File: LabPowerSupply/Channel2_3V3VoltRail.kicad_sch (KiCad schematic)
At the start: 8 parts

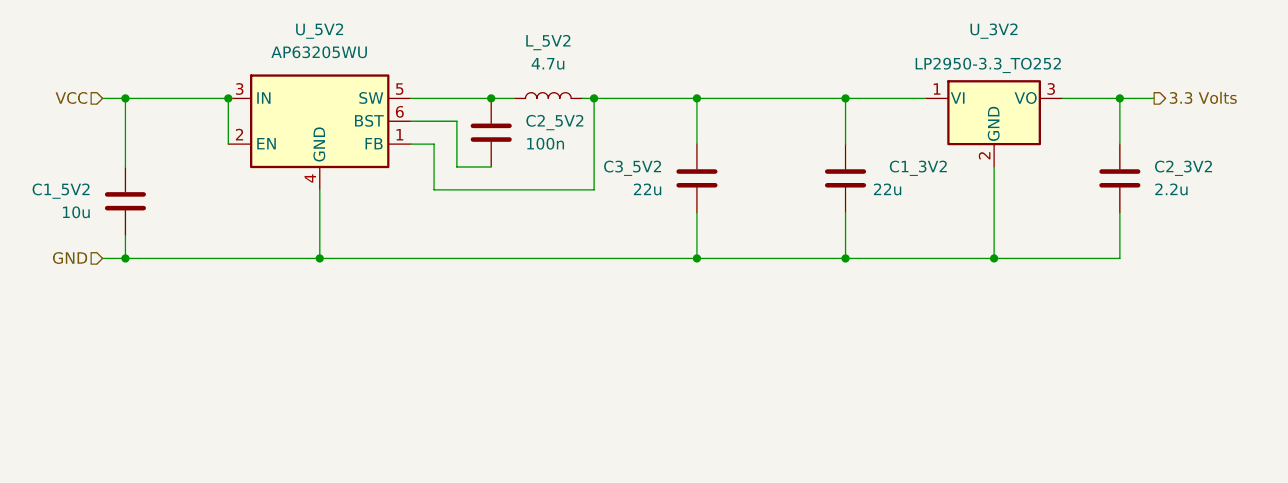
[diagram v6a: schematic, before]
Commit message: Updated Part List
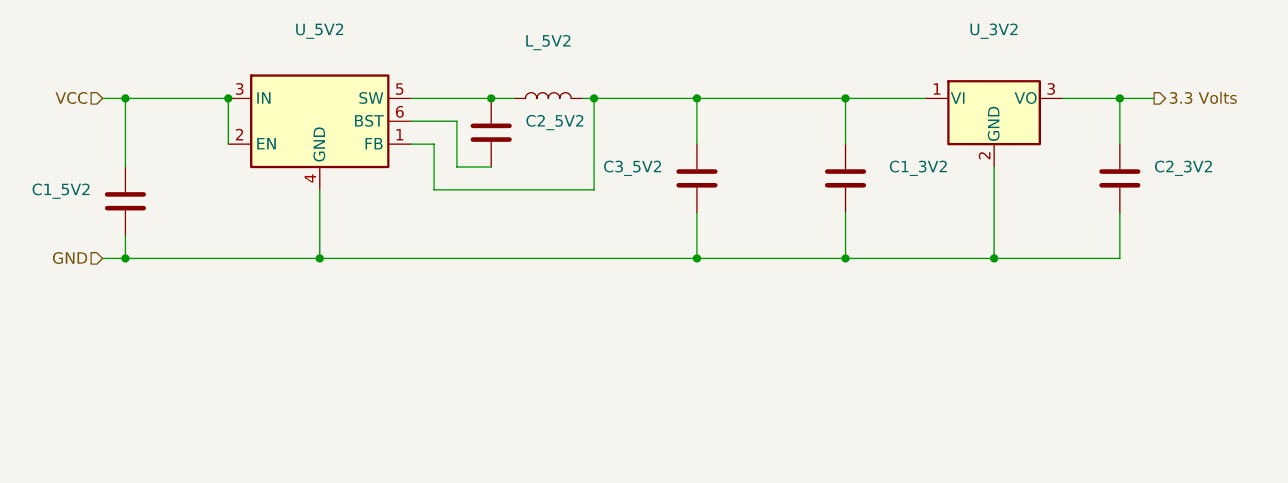
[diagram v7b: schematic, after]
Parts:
- C1_3V2, C3_5V2: value 22u -> (none); footprint Capacitor_SMD:C_1210_3225Metric -> (none)
- C1_5V2: value 10u -> (none); footprint Capacitor_SMD:C_1206_3216Metric -> (none)
- C2_3V2: value 2.2u -> (none); footprint Capacitor_SMD:C_0805_2012Metric -> (none)
- C2_5V2: value 100n -> (none); footprint Capacitor_SMD:C_0603_1608Metric -> (none)
- L_5V2: value 4.7u -> (none); footprint Inductor_SMD:L_Sumida_CDMC6D28_7.25x6.5mm -> (none)
- U_3V2: value LP2950-3.3_TO252 -> (none); footprint Package_TO_SOT_SMD:TO-252-2 -> (none)
- U_5V2: value AP63205WU -> (none); footprint Package_TO_SOT_SMD:TSOT-23-6 -> (none)
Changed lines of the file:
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@@
       (effects (font (size 1.27 1.27)) (justify left))
     )
-    (property "Value" "100n" (id 1) (at 160.02 74.9299 0)
+    (property "Value" "" (id 1) (at 160.02 74.9299 0)
       (effects (font (size 1.27 1.27)) (justify left))
     )
-    (property "Footprint" "Capacitor_SMD:C_0603_1608Metric" (id 2) (at 157.1752 77.47 0)
+    (property "Footprint" "" (id 2) (at 157.1752 77.47 0)
       (effects (font (size 1.27 1.27)) hide)
     )
@@
     (in_bom yes) (on_board yes) (fields_autoplaced)
     (property "Reference" "U_5V2" (id 0) (at 137.16 62.23 0))
-    (property "Value" "AP63205WU" (id 1) (at 137.16 64.77 0))
-    (property "Footprint" "Package_TO_SOT_SMD:TSOT-23-6" (id 2) (at 137.16 95.25 0)
+    (property "Value" "" (id 1) (at 137.16 64.77 0))
+    (property "Footprint" "" (id 2) (at 137.16 95.25 0)
       (effects (font (size 1.27 1.27)) hide)
     )
@@
       (effects (font (size 1.27 1.27)) (justify right))
     )
-    (property "Value" "22u" (id 1) (at 201.93 80.01 0)
+    (property "Value" "" (id 1) (at 201.93 80.01 0)
       (effects (font (size 1.27 1.27)) (justify right))
     )
-    (property "Footprint" "Capacitor_SMD:C_1210_3225Metric" (id 2) (at 196.5452 74.93 0)
+    (property "Footprint" "" (id 2) (at 196.5452 74.93 0)
       (effects (font (size 1.27 1.27)) hide)
     )
@@
     (in_bom yes) (on_board yes)
     (property "Reference" "U_3V2" (id 0) (at 212.09 62.23 0))
-    (property "Value" "LP2950-3.3_TO252" (id 1) (at 203.2 66.04 0)
+    (property "Value" "" (id 1) (at 203.2 66.04 0)
       (effects (font (size 1.27 1.27)) (justify left))
     )
-    (property "Footprint" "Package_TO_SOT_SMD:TO-252-2" (id 2) (at 212.09 64.135 0)
+    (property "Footprint" "" (id 2) (at 212.09 64.135 0)
       (effects (font (size 1.27 1.27) italic) hide)
     )
@@
     (in_bom yes) (on_board yes) (fields_autoplaced)
     (property "Reference" "L_5V2" (id 0) (at 162.56 63.5 90))
-    (property "Value" "4.7u" (id 1) (at 162.56 66.04 90))
-    (property "Footprint" "Inductor_SMD:L_Sumida_CDMC6D28_7.25x6.5mm" (id 2) (at 162.56 69.85 0)
+    (property "Value" "" (id 1) (at 162.56 66.04 90))
+    (property "Footprint" "" (id 2) (at 162.56 69.85 0)
       (effects (font (size 1.27 1.27)) hide)
     )
@@
       (effects (font (size 1.27 1.27)) (justify right))
     )
-    (property "Value" "22u" (id 1) (at 175.26 80.0099 0)
+    (property "Value" "" (id 1) (at 175.26 80.0099 0)
       (effects (font (size 1.27 1.27)) (justify right))
     )
-    (property "Footprint" "Capacitor_SMD:C_1210_3225Metric" (id 2) (at 180.0352 74.93 0)
+    (property "Footprint" "" (id 2) (at 180.0352 74.93 0)
       (effects (font (size 1.27 1.27)) hide)
     )
@@
       (effects (font (size 1.27 1.27)) (justify left))
     )
-    (property "Value" "2.2u" (id 1) (at 229.87 80.0099 0)
+    (property "Value" "" (id 1) (at 229.87 80.0099 0)
       (effects (font (size 1.27 1.27)) (justify left))
     )
-    (property "Footprint" "Capacitor_SMD:C_0805_2012Metric" (id 2) (at 227.0252 82.55 0)
+    (property "Footprint" "" (id 2) (at 227.0252 82.55 0)
       (effects (font (size 1.27 1.27)) hide)
     )
@@
       (effects (font (size 1.27 1.27)) (justify right))
     )
-    (property "Value" "10u" (id 1) (at 111.76 82.5499 0)
+    (property "Value" "" (id 1) (at 111.76 82.5499 0)
       (effects (font (size 1.27 1.27)) (justify right))
     )
-    (property "Footprint" "Capacitor_SMD:C_1206_3216Metric" (id 2) (at 116.5352 77.47 0)
+    (property "Footprint" "" (id 2) (at 116.5352 77.47 0)
       (effects (font (size 1.27 1.27)) hide)
     )
